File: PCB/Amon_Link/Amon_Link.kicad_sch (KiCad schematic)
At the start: 100 parts, among them IC1 SPX5205M5-L/TR, J1 USB_C_Receptacle_USB2.0, J2 SMA Edge, J3 Programing port, J4 SMA Edge, SW1 SW_SPST, U1 CH32V003F4P6, U2 CH340G, U3 NRF24L01, U4 RFX2401C, U5 NRF24L01, U6 RFX2401C, Y2 12MHz, Y3 16MHz, Y4 16MHz, Y5 24MHz

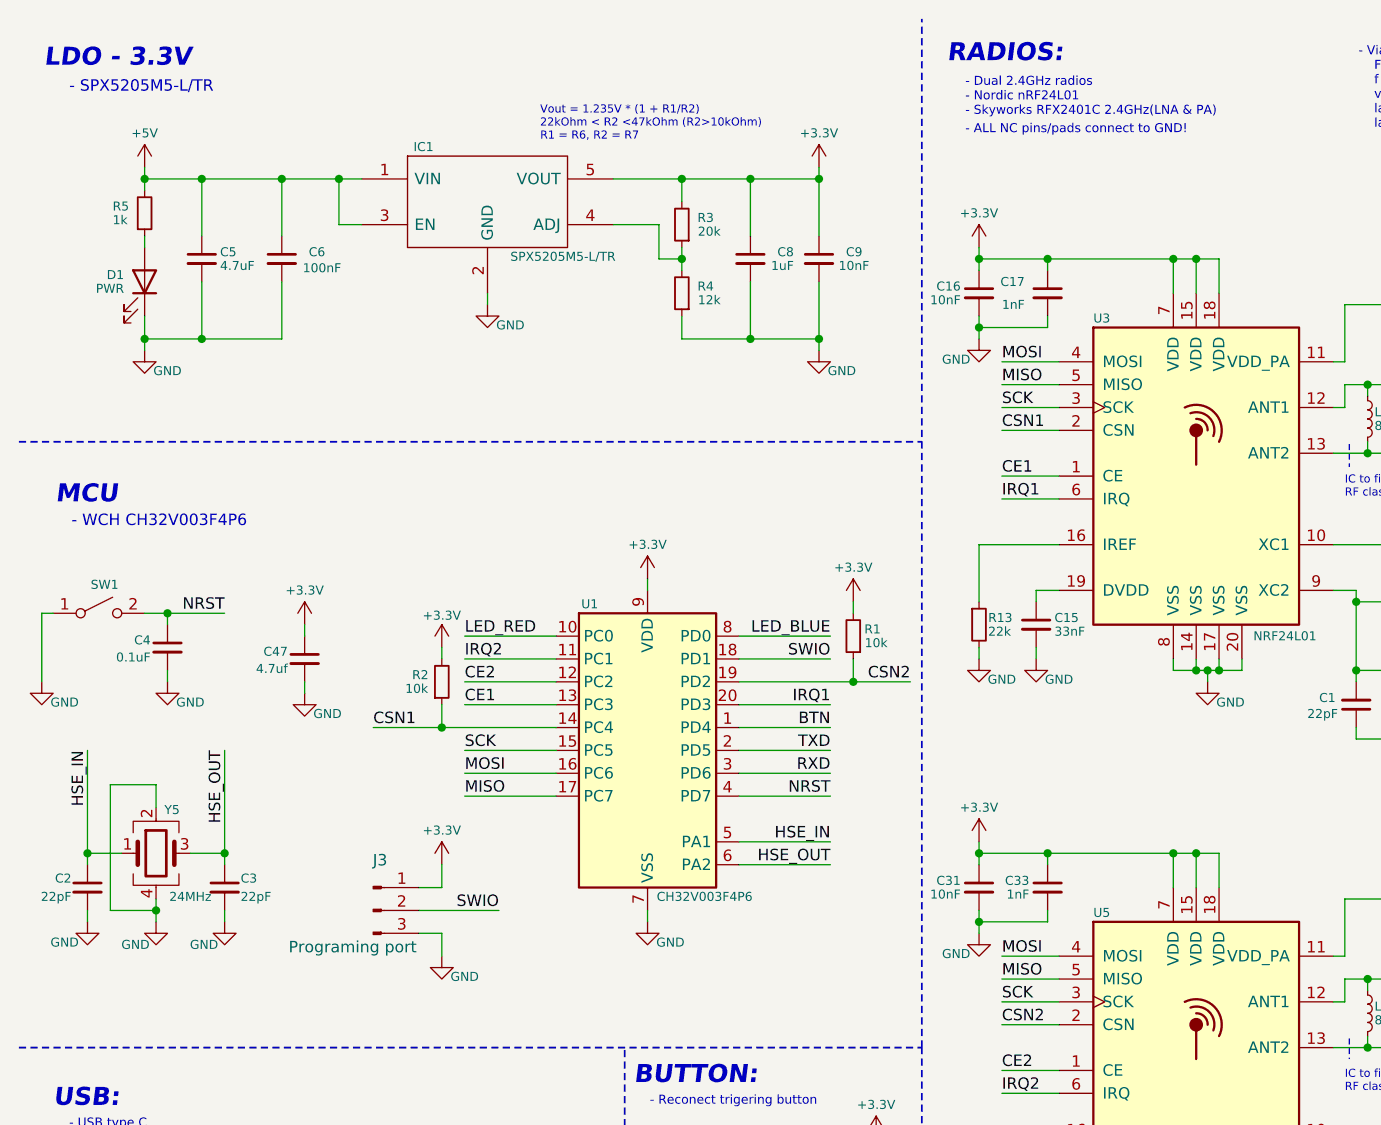
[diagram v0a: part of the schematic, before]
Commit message: Update
power stability optimization on PCB - added Cs for TX event
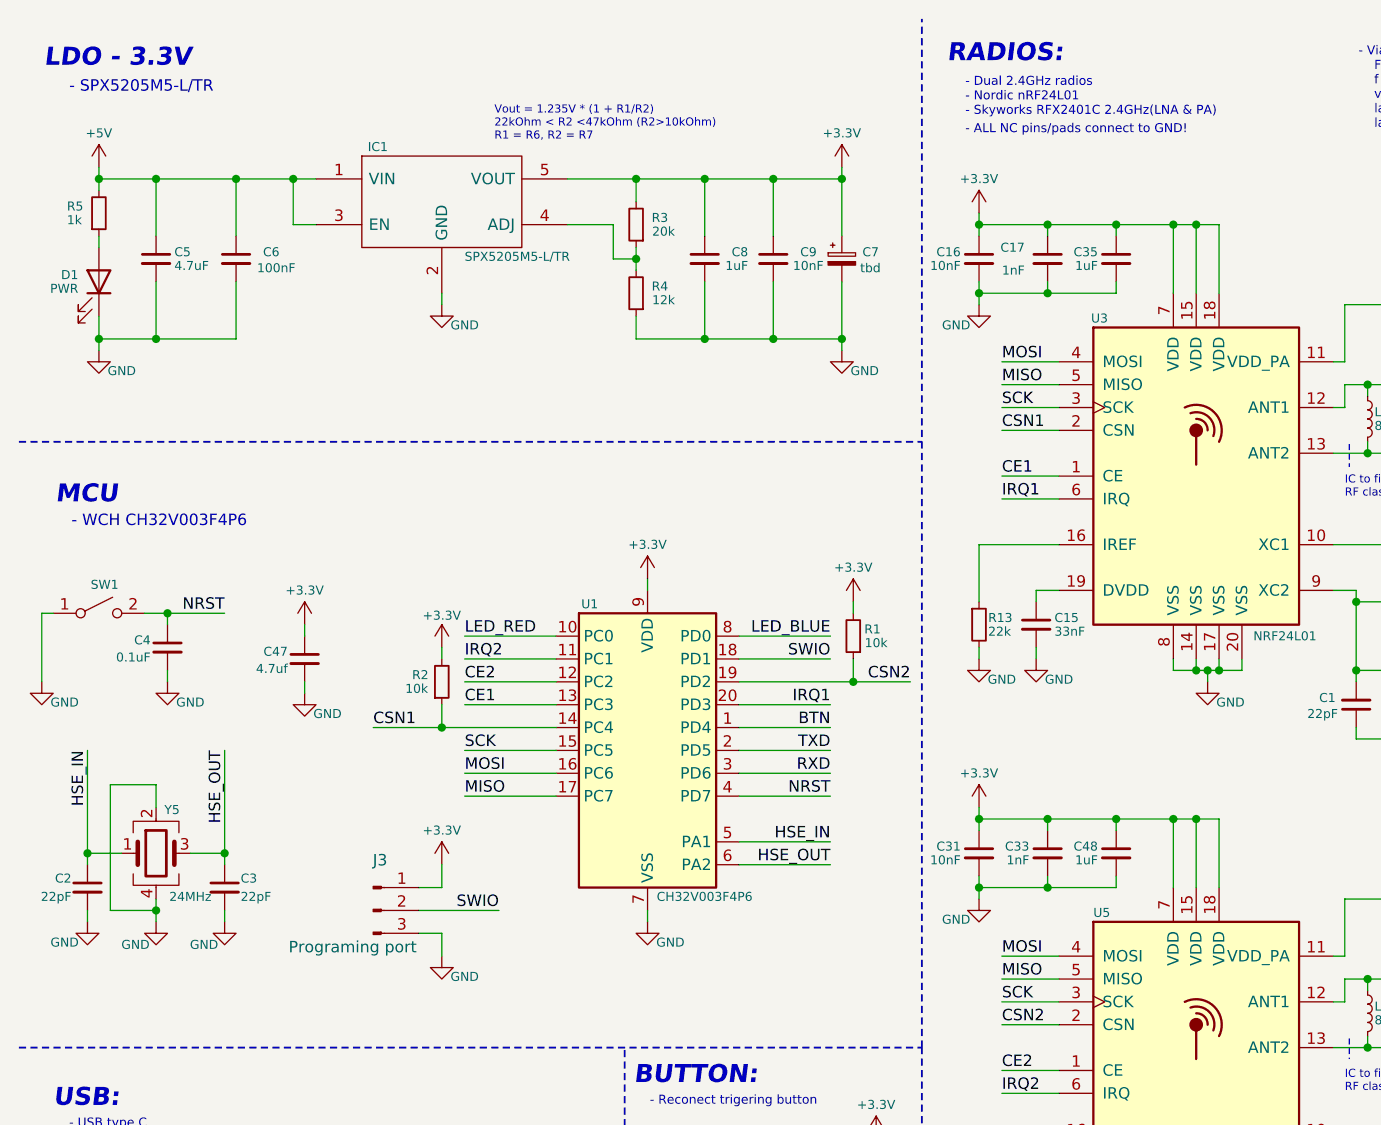
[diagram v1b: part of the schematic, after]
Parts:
- added C35, C48: 1uF, Capacitor_SMD:C_0402_1005Metric, symbol Device:C_Small
- added C7: tbd, Capacitor_Tantalum_SMD:CP_EIA-3528-12_Kemet-T, symbol Device:C_Polarized_Small
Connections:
- net +3.3V: now also C35.1, C48.1, C7.1
- net GND: now also C35.2, C48.2, C7.2
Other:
- moved on the sheet: C16, C17, C31, C33, C5, C6, C8, C9, D1, IC1, R3, R4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

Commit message: Images
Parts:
- R14, R19: now not fitted
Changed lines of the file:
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@@
 		(in_bom yes)
 		(on_board yes)
-		(dnp no)
+		(dnp yes)
 		(property "Reference" "R19"
 			(at 170.434 152.908 90)
@@
 		(in_bom yes)
 		(on_board yes)
-		(dnp no)
+		(dnp yes)
 		(property "Reference" "R14"
 			(at 170.434 86.868 90)
